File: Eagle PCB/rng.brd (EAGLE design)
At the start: 68.6 x 53.3 mm, 14 parts, among them IC1 U3V12F12, T1 2N3904, T2 2N3904, T3 2N3904

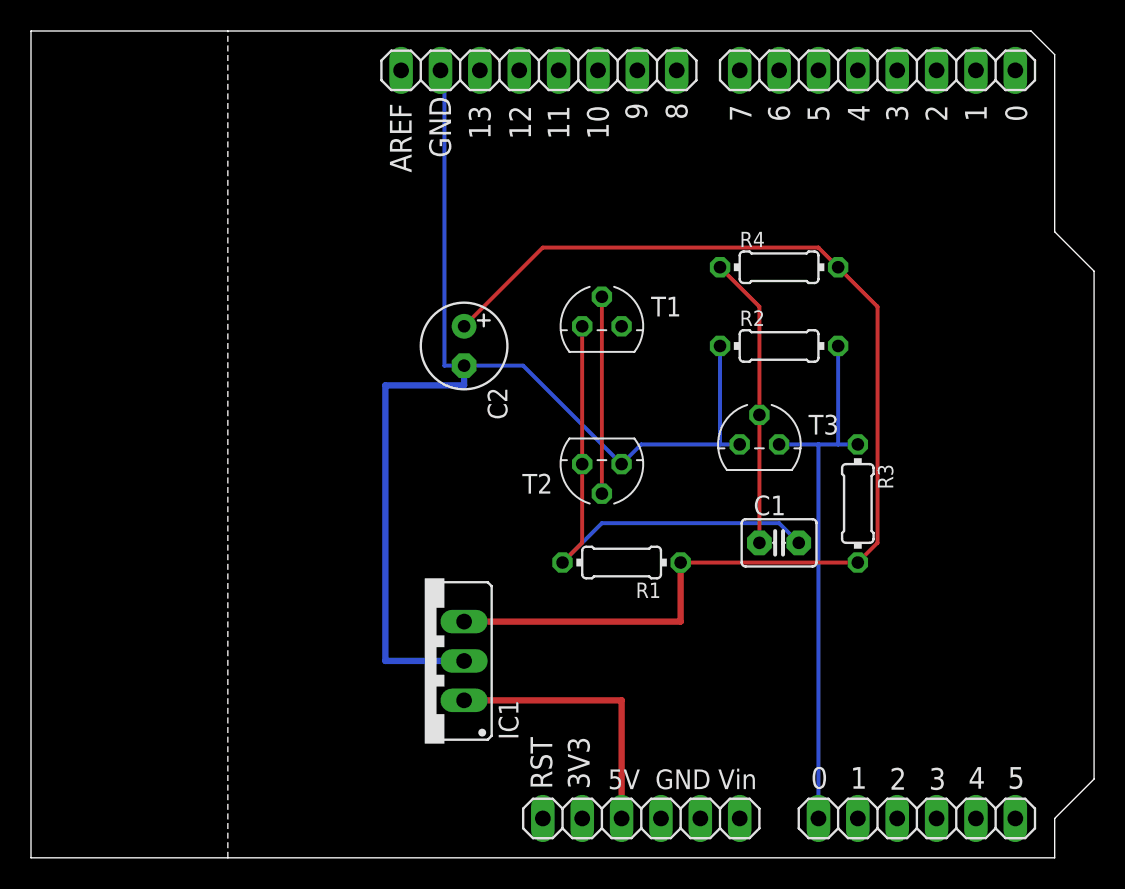
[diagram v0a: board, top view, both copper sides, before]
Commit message: make C1 lead spacing longer.  adjust layers, silkscreen, and trace widths.  no functional changes vs. v2.0.
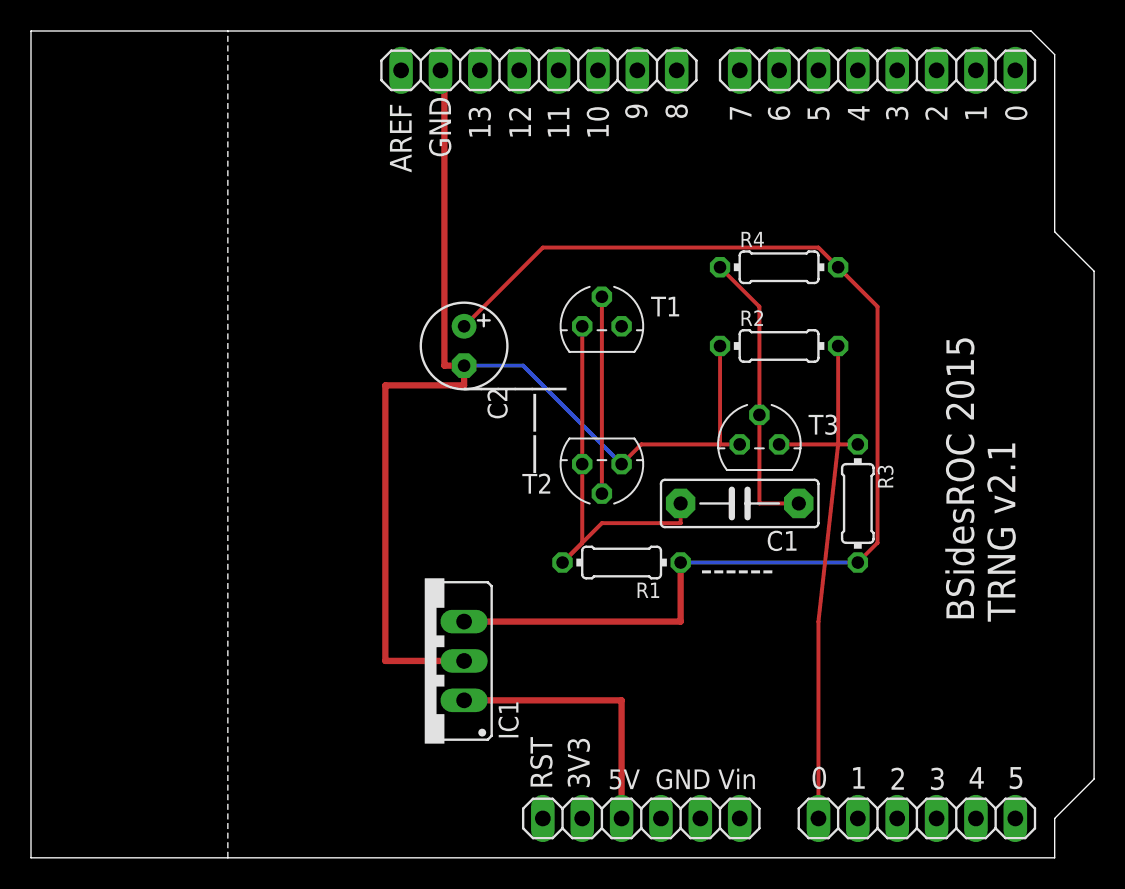
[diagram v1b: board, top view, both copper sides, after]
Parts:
- C1: device capacitor-wima:C2.5-3 -> capacitor-wima:C7.5B3
- moved C1 3.59 mm to (45.7, 22.9), turned to 180 degrees
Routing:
- net N$3: track 32.6 -> 25.7 mm
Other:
- board text added: "------"
- board text added: "BSidesROC 2015 TRNG v2.1"
- board text added: "______ | |"
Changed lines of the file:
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@@
 <text x="39.7488" y="47.6118" size="1.4" layer="25" font="fixed" rot="R90">9</text>
 <text x="42.3523" y="47.6118" size="1.4" layer="25" font="fixed" rot="R90">8</text>
+<text x="63.5" y="15.24" size="1.778" layer="25" rot="R90">BSidesROC 2015
+TRNG v2.1</text>
+<text x="43.18" y="17.78" size="1.778" layer="25">------</text>
+<text x="27.94" y="25.4" size="1.778" layer="25">______
+      |
+      |</text>
 </plain>
 <attributes>
@@
 <element name="T3" library="transistor" package="TO92" value="2N3904" x="46.99" y="26.67"/>
 <element name="R1" library="rcl" package="0204/7" value="4.7k" x="38.1" y="19.05" rot="R180"/>
-<element name="C1" library="capacitor-wima" package="C2.5-3" value="0.1µf" x="48.26" y="20.32"/>
+<element name="C1" library="capacitor-wima" package="C7.5B3" value="0.1µf" x="45.72" y="22.86" rot="R180"/>
 <element name="R2" library="rcl" package="0204/7" value="4.7K" x="48.26" y="33.02"/>
 <element name="R3" library="rcl" package="0204/7" value="10k" x="53.34" y="22.86" rot="R270"/>
@@
 <wire x1="35.56" y1="20.32" x2="35.56" y2="25.4" width="0.254" layer="1"/>
 <wire x1="35.56" y1="25.4" x2="35.56" y2="34.29" width="0.254" layer="1"/>
-<wire x1="48.26" y1="21.59" x2="49.53" y2="20.32" width="0.254" layer="16"/>
-<wire x1="36.83" y1="21.59" x2="48.26" y2="21.59" width="0.254" layer="16"/>
-<wire x1="34.29" y1="19.05" x2="36.83" y2="21.59" width="0.254" layer="16"/>
+<wire x1="34.29" y1="19.05" x2="36.83" y2="21.59" width="0.254" layer="1"/>
+<wire x1="36.83" y1="21.59" x2="41.91" y2="21.59" width="0.254" layer="1"/>
+<wire x1="41.91" y1="21.59" x2="41.91" y2="22.86" width="0.254" layer="1"/>
 </signal>
 <signal name="N$4">
@@
 <contactref element="R4" pad="2"/>
 <contactref element="C2" pad="+"/>
-<wire x1="41.91" y1="19.05" x2="53.34" y2="19.05" width="0.254" layer="1"/>
+<wire x1="41.91" y1="19.05" x2="53.34" y2="19.05" width="0.254" layer="16"/>
 <wire x1="54.61" y1="35.56" x2="52.07" y2="38.1" width="0.254" layer="1"/>
 <wire x1="54.61" y1="20.32" x2="54.61" y2="35.56" width="0.254" layer="1"/>
@@
 <contactref element="C1" pad="1"/>
 <contactref element="R4" pad="1"/>
-<wire x1="46.99" y1="20.32" x2="46.99" y2="28.575" width="0.254" layer="1"/>
 <wire x1="46.99" y1="35.56" x2="44.45" y2="38.1" width="0.254" layer="1"/>
 <wire x1="46.99" y1="28.575" x2="46.99" y2="35.56" width="0.254" layer="1"/>
+<wire x1="49.53" y1="22.86" x2="46.99" y2="22.86" width="0.254" layer="1"/>
+<wire x1="46.99" y1="22.86" x2="46.99" y2="28.575" width="0.254" layer="1"/>
 </signal>
 <signal name="N$6">
@@
 <contactref element="T3" pad="1"/>
 <contactref element="U$2" pad="1"/>
-<wire x1="52.07" y1="26.67" x2="53.34" y2="26.67" width="0.254" layer="16"/>
-<wire x1="50.8" y1="26.67" x2="52.07" y2="26.67" width="0.254" layer="16"/>
-<wire x1="50.8" y1="26.67" x2="48.26" y2="26.67" width="0.254" layer="16"/>
-<wire x1="52.07" y1="26.67" x2="52.07" y2="33.02" width="0.254" layer="16"/>
-<wire x1="50.8" y1="2.54" x2="50.8" y2="26.67" width="0.254" layer="16"/>
+<wire x1="52.07" y1="26.67" x2="53.34" y2="26.67" width="0.254" layer="1"/>
+<wire x1="52.07" y1="26.67" x2="48.26" y2="26.67" width="0.254" layer="1"/>
+<wire x1="52.07" y1="26.67" x2="52.07" y2="33.02" width="0.254" layer="1"/>
+<wire x1="52.07" y1="26.67" x2="50.8" y2="15.24" width="0.254" layer="1"/>
+<wire x1="50.8" y1="15.24" x2="50.8" y2="2.54" width="0.254" layer="1"/>
 </signal>
 <signal name="N$7">
@@
 <contactref element="R2" pad="1"/>
 <contactref element="C2" pad="-"/>
-<wire x1="38.1" y1="25.4" x2="39.37" y2="26.67" width="0.254" layer="16"/>
-<wire x1="44.45" y1="26.67" x2="45.72" y2="26.67" width="0.254" layer="16"/>
-<wire x1="39.37" y1="26.67" x2="44.45" y2="26.67" width="0.254" layer="16"/>
-<wire x1="44.45" y1="26.67" x2="44.45" y2="33.02" width="0.254" layer="16"/>
-<wire x1="26.67" y1="31.75" x2="26.67" y2="49.53" width="0.254" layer="16"/>
-<wire x1="26.67" y1="31.75" x2="27.94" y2="31.75" width="0.254" layer="16"/>
-<wire x1="26.67" y1="49.53" x2="26.416" y2="50.8" width="0.254" layer="16"/>
+<wire x1="38.1" y1="25.4" x2="39.37" y2="26.67" width="0.254" layer="1"/>
+<wire x1="44.45" y1="26.67" x2="45.72" y2="26.67" width="0.254" layer="1"/>
+<wire x1="39.37" y1="26.67" x2="44.45" y2="26.67" width="0.254" layer="1"/>
+<wire x1="44.45" y1="26.67" x2="44.45" y2="33.02" width="0.254" layer="1"/>
+<wire x1="26.67" y1="31.75" x2="26.67" y2="49.53" width="0.4064" layer="1"/>
+<wire x1="26.67" y1="31.75" x2="27.94" y2="31.75" width="0.4064" layer="1"/>
+<wire x1="26.67" y1="49.53" x2="26.416" y2="50.8" width="0.4064" layer="1"/>
 <wire x1="31.75" y1="31.75" x2="38.1" y2="25.4" width="0.254" layer="16"/>
 <wire x1="27.94" y1="31.75" x2="31.75" y2="31.75" width="0.254" layer="16"/>
-<wire x1="27.94" y1="12.7" x2="22.86" y2="12.7" width="0.4064" layer="16"/>
-<wire x1="22.86" y1="12.7" x2="22.86" y2="30.48" width="0.4064" layer="16"/>
-<wire x1="22.86" y1="30.48" x2="27.94" y2="30.48" width="0.4064" layer="16"/>
-<wire x1="27.94" y1="30.48" x2="27.94" y2="31.75" width="0.4064" layer="16"/>
+<wire x1="27.94" y1="12.7" x2="22.86" y2="12.7" width="0.4064" layer="1"/>
+<wire x1="22.86" y1="12.7" x2="22.86" y2="30.48" width="0.4064" layer="1"/>
+<wire x1="22.86" y1="30.48" x2="27.94" y2="30.48" width="0.4064" layer="1"/>
+<wire x1="27.94" y1="30.48" x2="27.94" y2="31.75" width="0.4064" layer="1"/>
 </signal>
 </signals>
 </board>
 </drawing>
+<compatibility>
+<note version="6.3" minversion="6.2.2" severity="warning">
+Since Version 6.2.2 text objects can contain more than one line,
+which will not be processed correctly with this version.
+</note>
+</compatibility>
 </eagle>
